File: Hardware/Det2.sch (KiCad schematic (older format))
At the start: 11 parts

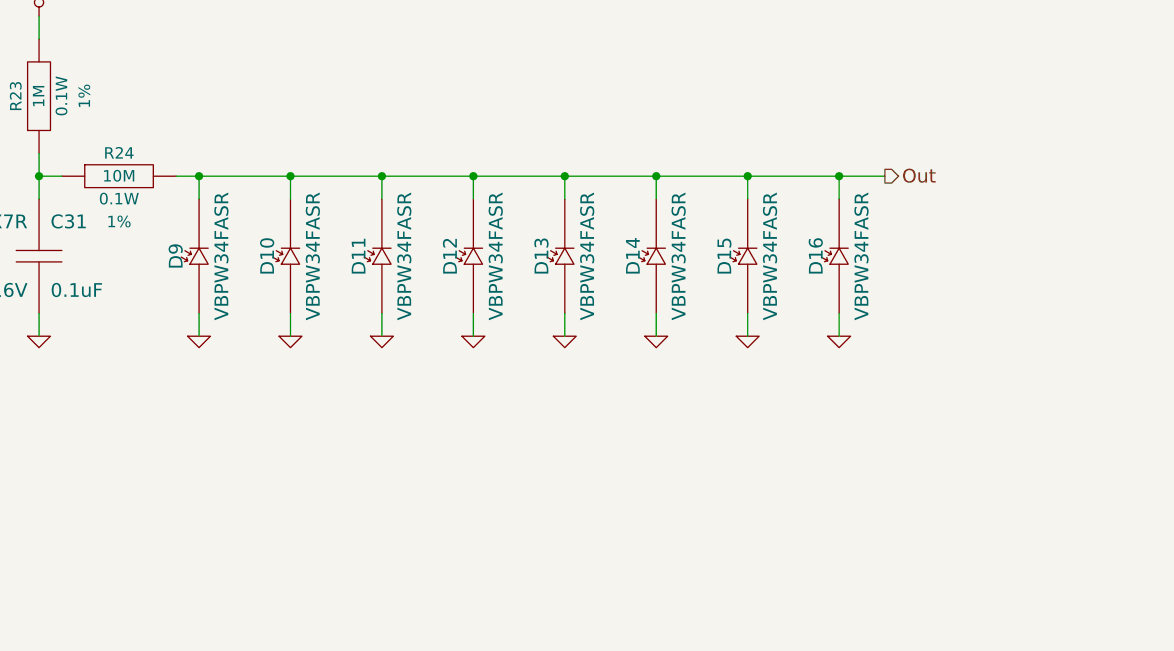
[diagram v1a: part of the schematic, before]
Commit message: Add additional photodiodes
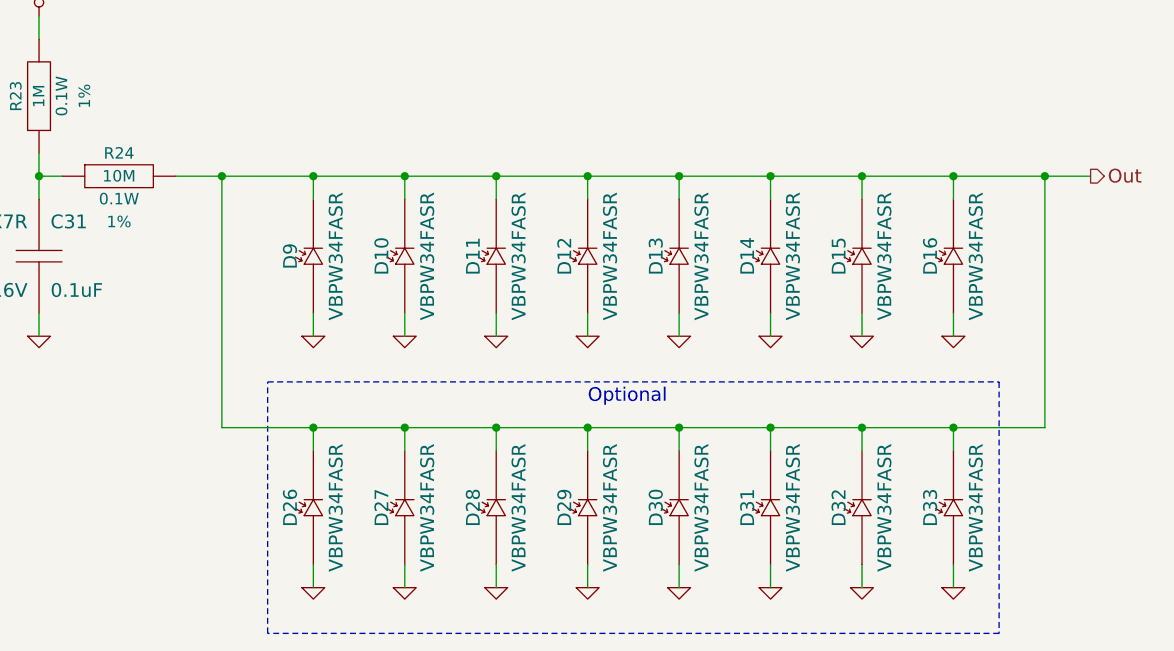
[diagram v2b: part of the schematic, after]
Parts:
- added D26, D27, D28, D29, D30, D31, D32, D33: VBPW34FASR, DIOC-BPW34R, symbol DIODE-PHOTO
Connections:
- net GND: now also D26.1, D27.1, D28.1, D29.1, D30.1, D31.1, D32.1, D33.1
- net Out: now also D26.2, D27.2, D28.2, D29.2, D30.2, D31.2, D32.2, D33.2
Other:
- note added: "Optional"
- moved on the sheet: D10, D11, D12, D13, D14, D15, D16, D9

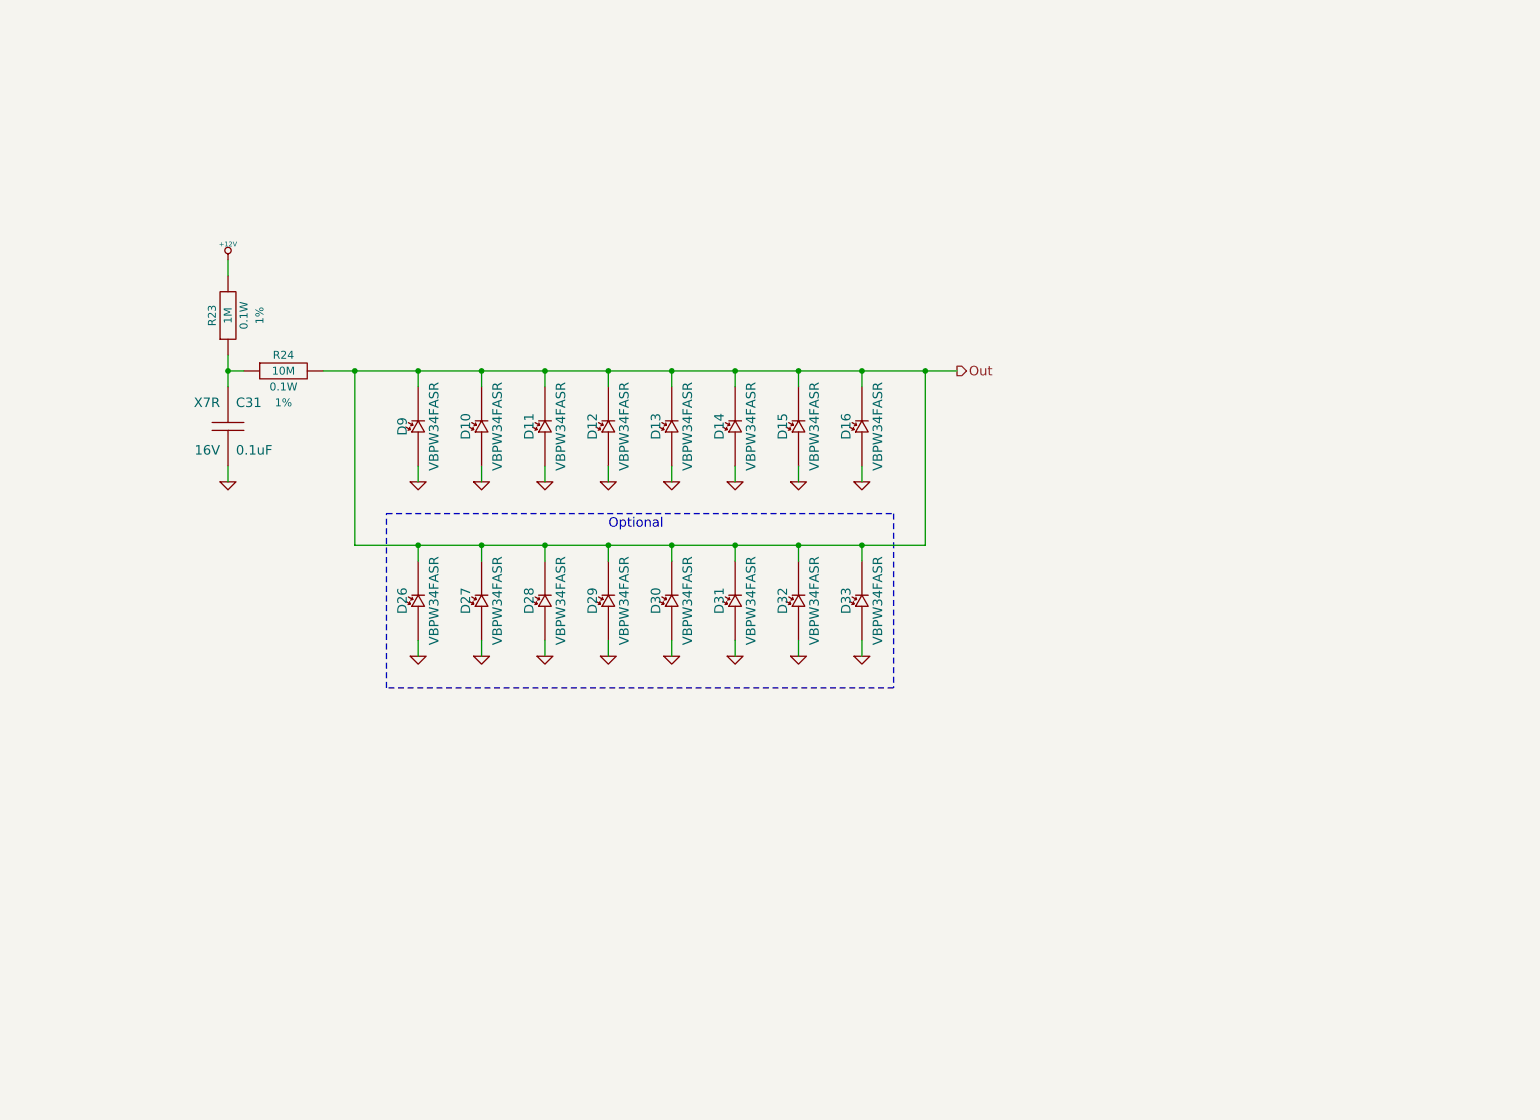
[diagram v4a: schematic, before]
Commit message: Move amplifiers into detection subsheets
Reannotate
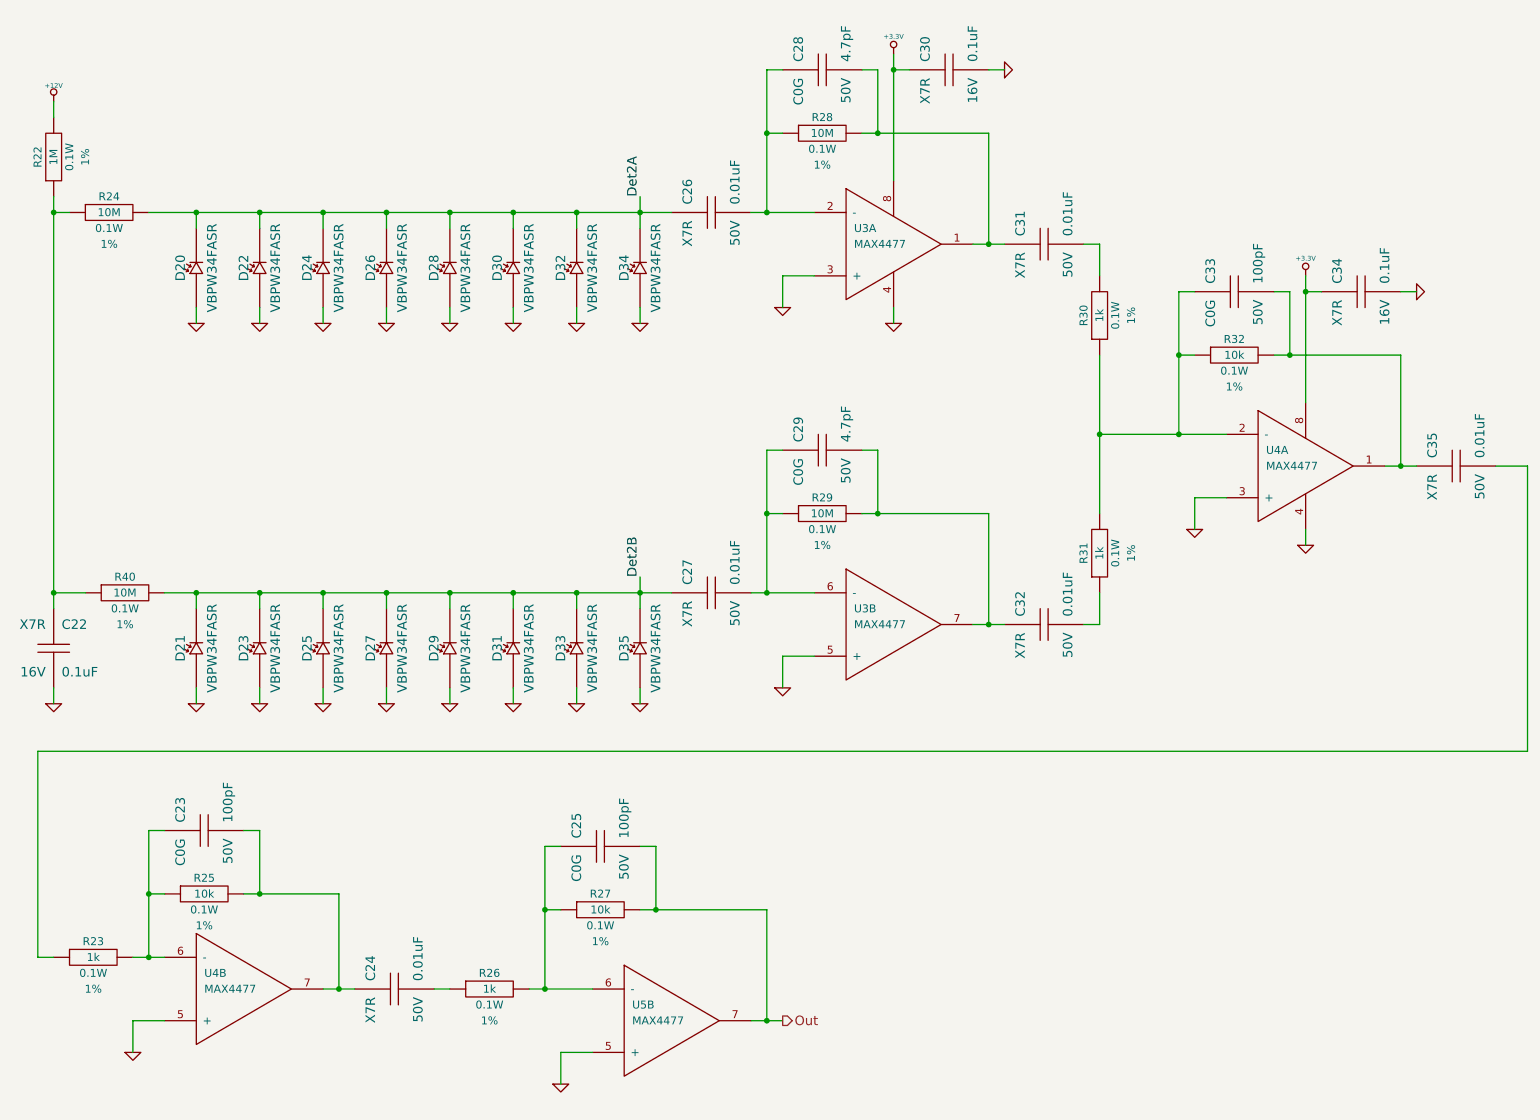
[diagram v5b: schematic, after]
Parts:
- removed D10, D11, D12, D13, D14, D15, D16, D9: VBPW34FASR, DIOC-BPW34R, symbol DIODE-PHOTO
- added C22, C30, C34: 0.1uF, CAPC1608, symbol C
- added C23, C25, C33: 100pF, CAPC1608, symbol C
- added C24, C26, C27, C32, C35: 0.01uF, CAPC1608, symbol C
- added C28, C29: 4.7pF, CAPC1608, symbol C
- added D20, D21, D22, D23, D24, D25, D34, D35: VBPW34FASR, DIOC-BPW34R, symbol DIODE-PHOTO
- added R22: 1M, RESC1608, symbol R
- added R25, R27, R32: 10k, RESC1608, symbol R
- added R26, R30, R31: 1k, RESC1608, symbol R
- added R28, R29, R40: 10M, RESC1608, symbol R
- added U3, U4, U5: MAX4477, symbol OPAMP-DUAL
- C31: value 0.1uF -> 0.01uF; Distributor Part No 1276-1005-1-ND -> 1276-1921-1-ND; MFR Part No CL10B104KO8NNNC -> CL10B103KB8NCNC; Voltage 16V -> 50V
- R23: value 1M -> 1k; Distributor Part No 311-1.00MHRCT-ND -> 311-1.00KHRCT-ND; MFR Part No RC0603FR-071ML -> RC0603FR-071KL
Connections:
- net +12V: now also R22.2; no longer R23.2
- net GND: now also C22.2, C30.2, C34.2, D20.1, D21.1, D22.1, D23.1, D24.1, D25.1, D34.1, D35.1, U3.3 (+), U3.4, U3.5 (+), U4.3 (+), U4.4, U4.5 (+), U5.5 (+); no longer C31.2
- net Out: now also C25.2, R27.2, U5.7; no longer D26.2, D27.2, D28.2, D29.2, D30.2, D31.2, D32.2, D33.2, R24.2
- new net: C22.1, R22.1, R24.1, R40.1
- new net: C28.2, C31.1, R28.2, U3.1
- new net: C26.2, C28.1, R28.1, U3.2 (-)
- new net: C27.2, C29.1, R29.1, U3.6 (-)
- new net: C29.2, C32.1, R29.2, U3.7
- new net: C31.2, R30.2
- new net: C32.2, R31.1
- new net: C33.1, R30.1, R31.2, R32.1, U4.2 (-)
- new net: C23.1, R23.2, R25.1, U4.6 (-)
- new net: C23.2, C24.1, R25.2, U4.7
- new net: C24.2, R26.1
- new net: C33.2, C35.1, R32.2, U4.1
- new net: C35.2, R23.1
- new net: C25.1, R26.2, R27.1, U5.6 (-)
- new net +3.3V: C30.1, C34.1, U3.8, U4.8
- new net Det2A: C26.1, D20.2, D22.2, D24.2, D26.2, D28.2, D30.2, D32.2, D34.2, R24.2
- new net Det2B: C27.1, D21.2, D23.2, D25.2, D27.2, D29.2, D31.2, D33.2, D35.2, R40.2
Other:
- note removed: "Optional"
